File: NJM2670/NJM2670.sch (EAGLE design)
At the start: 10 parts, among them Q1 MOSFET-PCHANNELIRLML2244

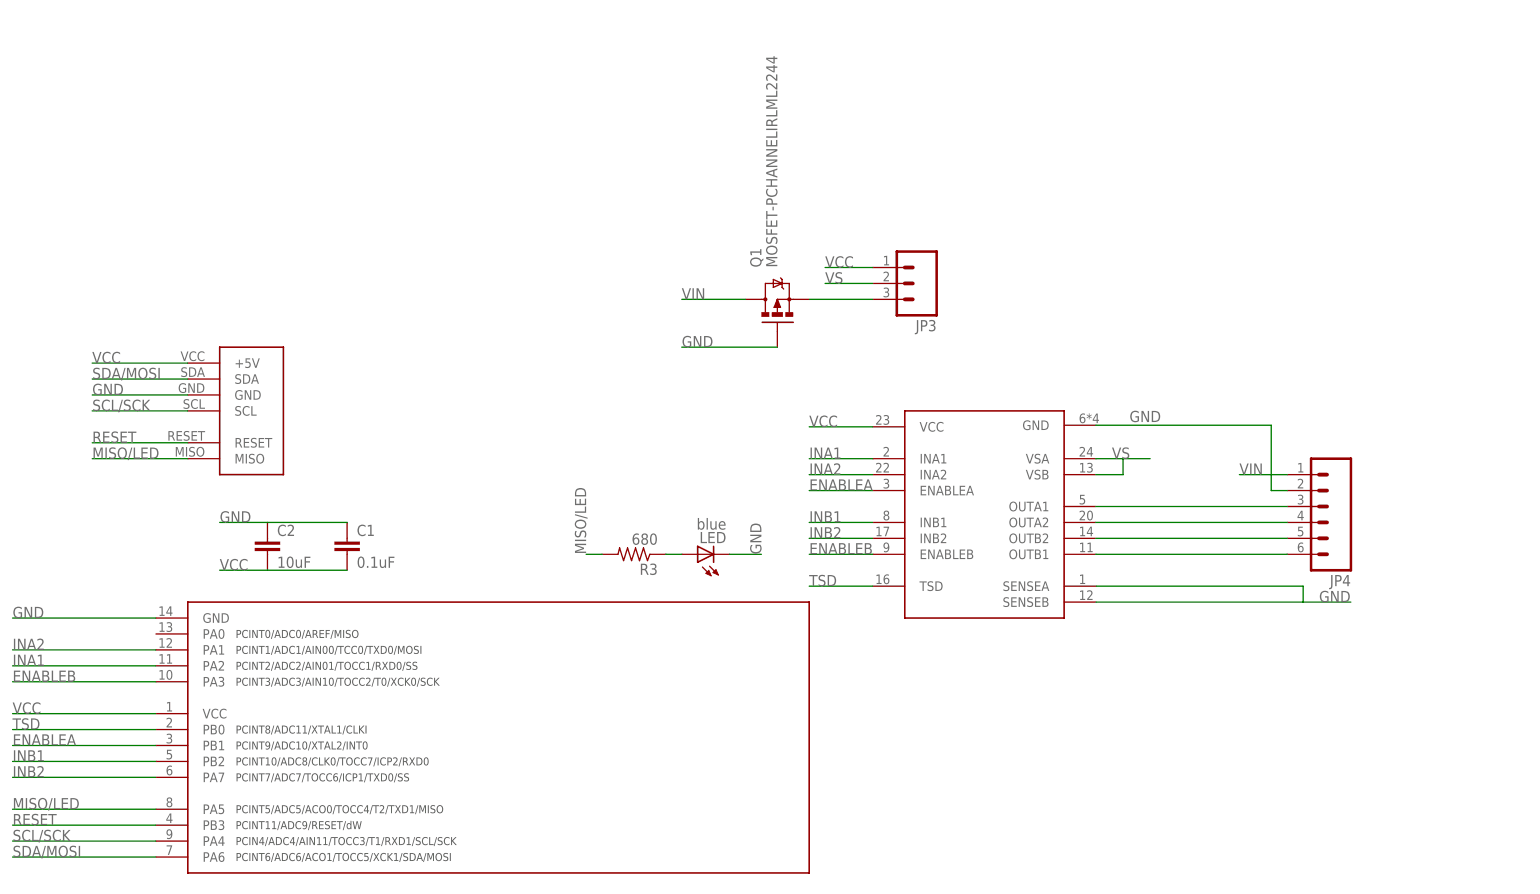
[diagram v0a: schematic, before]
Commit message: New linear/inline layout of motor driver board
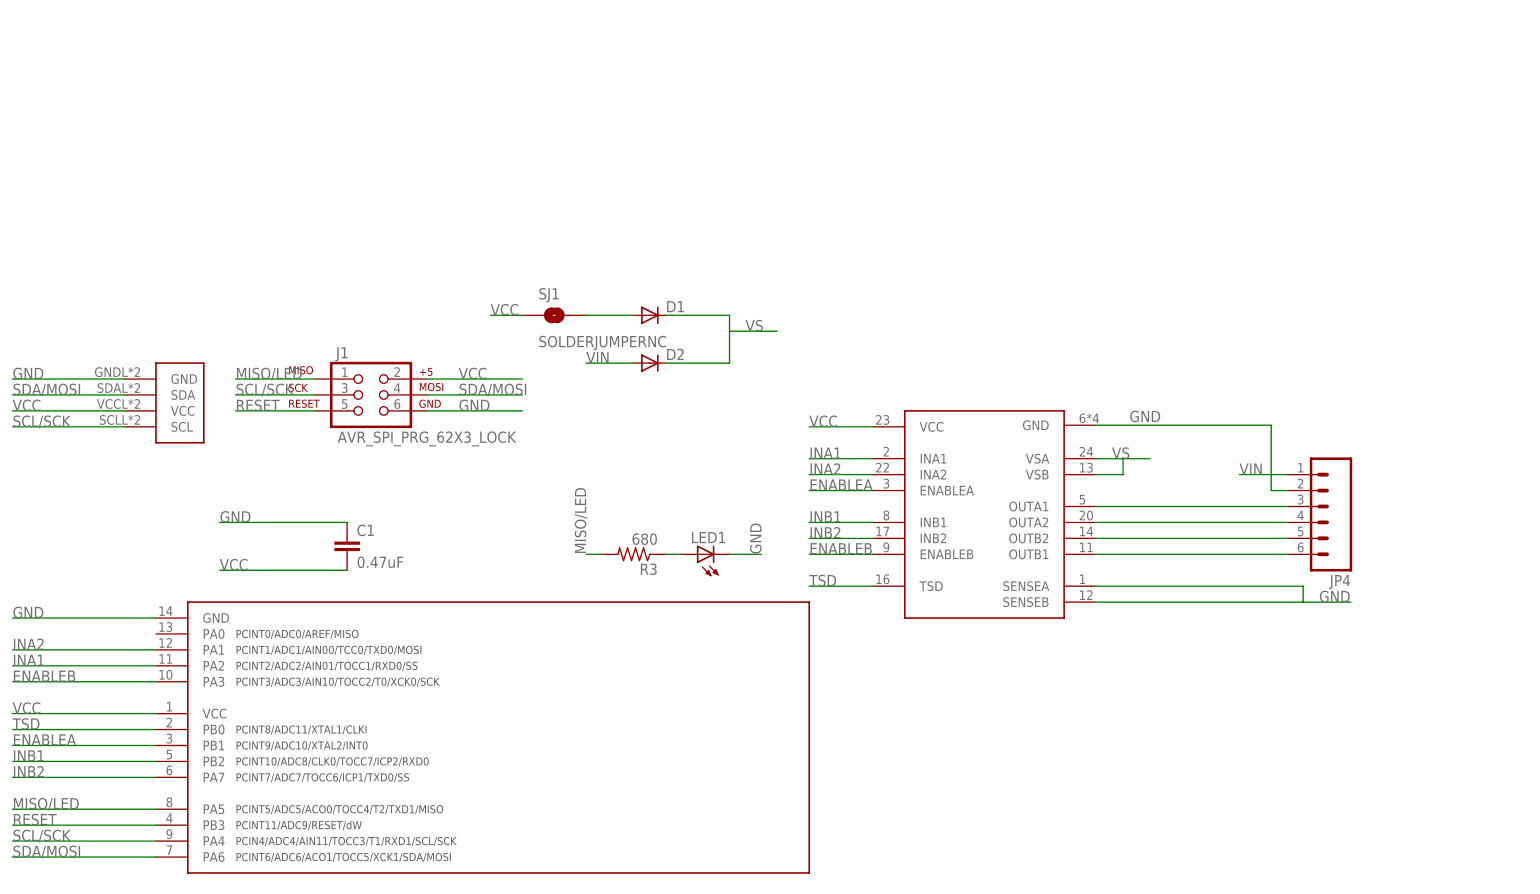
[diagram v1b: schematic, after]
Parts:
- removed C2: 10uF, SparkFun-Capacitors:CAP0805
- removed JP3: (no value), SparkFun-Connectors:M03PTH
- removed LED: blue, led:LEDCHIPLED_1206
- removed Q1: MOSFET-PCHANNELIRLML2244, SparkFun-DiscreteSemi:MOSFET-PCHANNELIRLML2244
- removed U$4: FOOTPRINTFOOTPRINT-2, IntegerLabs:FOOTPRINTFOOTPRINT-2
- added D1, D2: (no value), SparkFun-DiscreteSemi:DIODESMB
- added J1: AVR_SPI_PRG_62X3_LOCK, SparkFun-Connectors:AVR_SPI_PRG_62X3_LOCK
- added LED1: (no value), adafruit:LEDCHIPLED_0805
- added SJ1: SOLDERJUMPERNC, SparkFun-Passives:SOLDERJUMPERNC
- added U$1: FOOTPRINT3-4U, IntegerLabs:FOOTPRINT3-4U
- C1: value 0.1uF -> 0.47uF
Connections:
- net GND: now also J1.6, LED1.C, U$1.GND; no longer C2.1, LED.C, Q1.G, U$4.GND
- net MISO/LED: now also J1.1; no longer U$4.MISO
- net N$1: now also D1.A, SJ1.2; no longer JP3.3, Q1.S
- net N$5: now also LED1.A; no longer LED.A
- net RESET: now also J1.5; no longer U$4.RESET
- net SCL/SCK: now also J1.3, U$1.SCL; no longer U$4.SCL
- net SDA/MOSI: now also J1.4, U$1.SDA; no longer U$4.SDA
- net VCC: now also J1.2, SJ1.1, U$1.VCC; no longer C2.2, JP3.1, U$4.+5V
- net VIN: now also D2.A; no longer Q1.D
- net VS: now also D1.C, D2.C; no longer JP3.2

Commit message: Reverted to old version of motor driver board
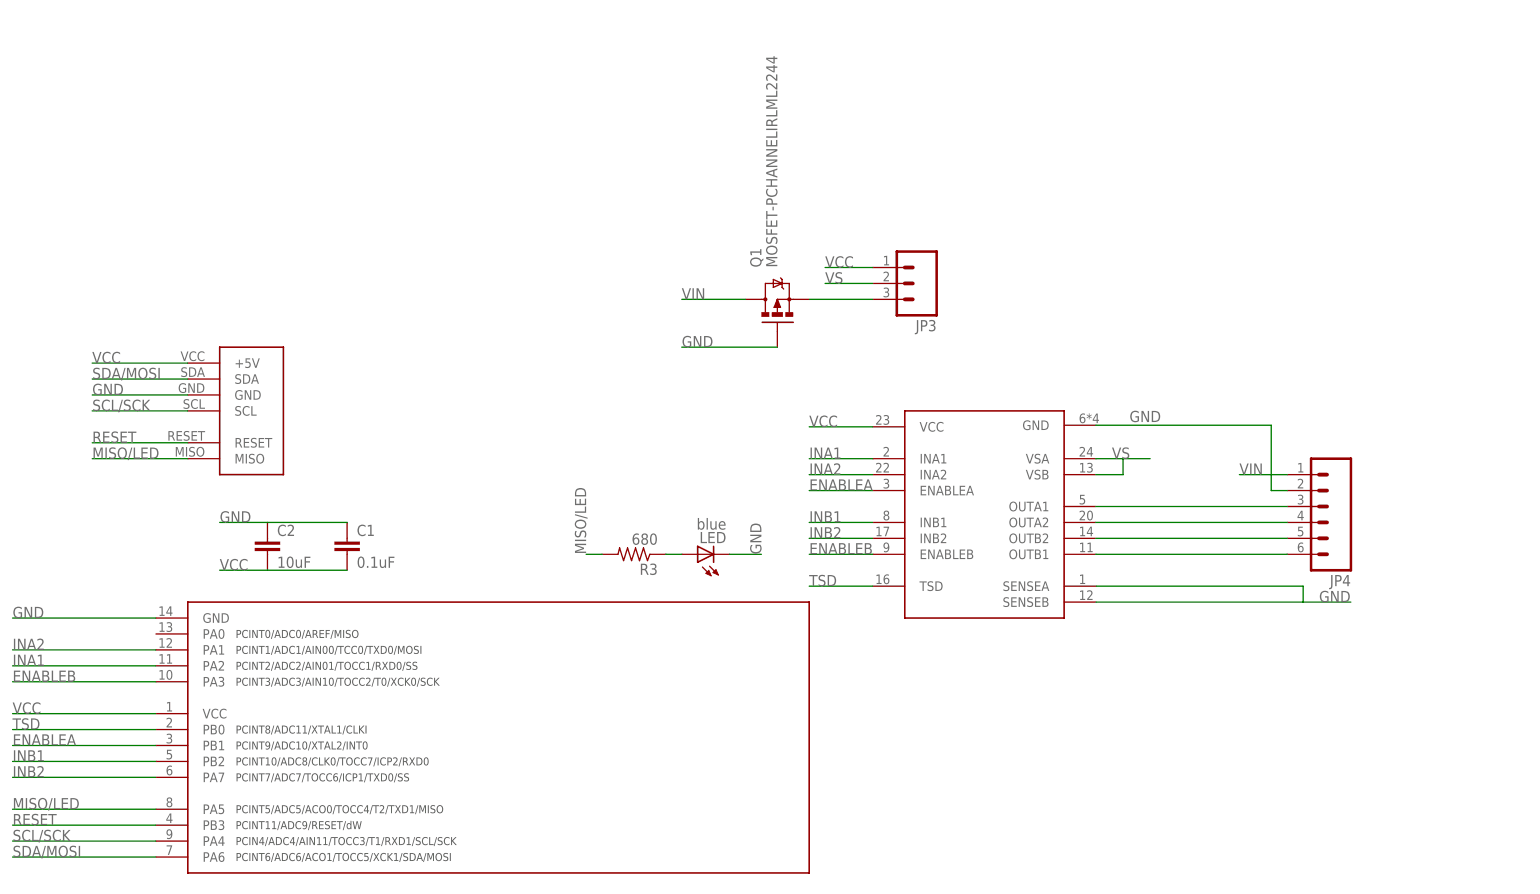
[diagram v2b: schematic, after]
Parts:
- removed D1, D2: (no value), SparkFun-DiscreteSemi:DIODESMB
- removed J1: AVR_SPI_PRG_62X3_LOCK, SparkFun-Connectors:AVR_SPI_PRG_62X3_LOCK
- removed LED1: (no value), adafruit:LEDCHIPLED_0805
- removed SJ1: SOLDERJUMPERNC, SparkFun-Passives:SOLDERJUMPERNC
- removed U$1: FOOTPRINT3-4U, IntegerLabs:FOOTPRINT3-4U
- added C2: 10uF, SparkFun-Capacitors:CAP0805
- added JP3: (no value), SparkFun-Connectors:M03PTH
- added LED: blue, led:LEDCHIPLED_1206
- added Q1: MOSFET-PCHANNELIRLML2244, SparkFun-DiscreteSemi:MOSFET-PCHANNELIRLML2244
- added U$4: FOOTPRINTFOOTPRINT-2, IntegerLabs:FOOTPRINTFOOTPRINT-2
- C1: value 0.47uF -> 0.1uF
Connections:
- net GND: now also C2.1, LED.C, Q1.G, U$4.GND; no longer J1.6, LED1.C, U$1.GND
- net MISO/LED: now also U$4.MISO; no longer J1.1
- net N$1: now also JP3.3, Q1.S; no longer D1.A, SJ1.2
- net N$5: now also LED.A; no longer LED1.A
- net RESET: now also U$4.RESET; no longer J1.5
- net SCL/SCK: now also U$4.SCL; no longer J1.3, U$1.SCL
- net SDA/MOSI: now also U$4.SDA; no longer J1.4, U$1.SDA
- net VCC: now also C2.2, JP3.1, U$4.+5V; no longer J1.2, SJ1.1, U$1.VCC
- net VIN: now also Q1.D; no longer D2.A
- net VS: now also JP3.2; no longer D1.C, D2.C

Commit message: Updated footprint and swich, instead of jumper, for selecting output voltage.
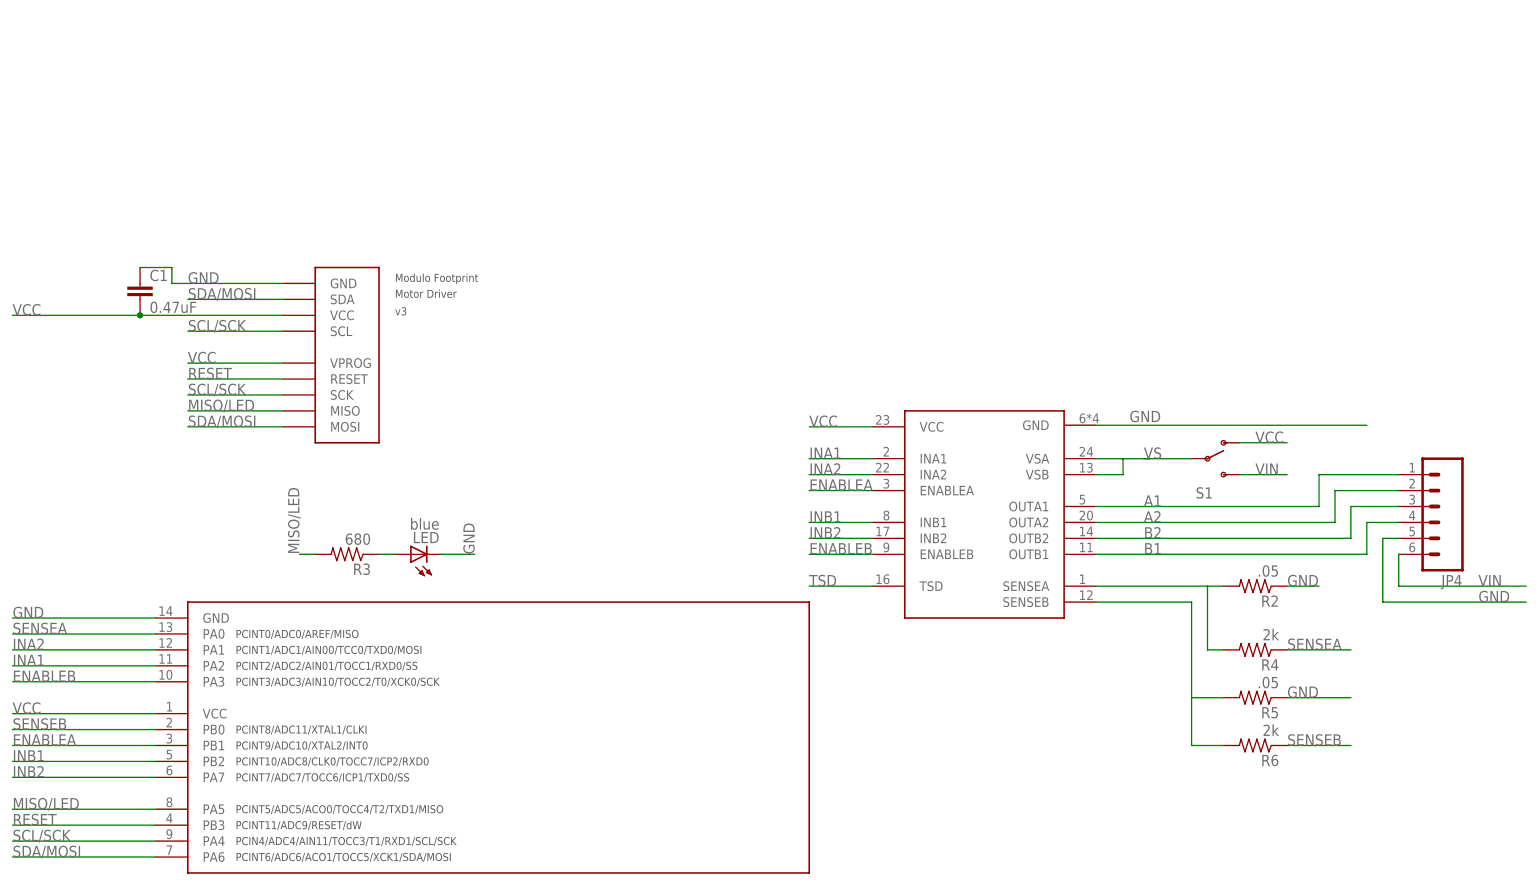
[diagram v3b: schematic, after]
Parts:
- removed C2: 10uF, SparkFun-Capacitors:CAP0805
- removed JP3: (no value), SparkFun-Connectors:M03PTH
- removed Q1: MOSFET-PCHANNELIRLML2244, SparkFun-DiscreteSemi:MOSFET-PCHANNELIRLML2244
- removed U$4: FOOTPRINTFOOTPRINT-2, IntegerLabs:FOOTPRINTFOOTPRINT-2
- added R2, R5: .05, SparkFun-Passives:RESISTOR0805-RES
- added R4, R6: 2k, SparkFun-Passives:RESISTOR0805-RES
- added S1: (no value), SparkFun-Electromechanical:SWITCH-SPDTPTH_LOCK
- added U$1: FOOTPRINTFOOTPRINT-2, IntegerLabs:FOOTPRINTFOOTPRINT-2
- C1: value 0.1uF -> 0.47uF
- LED: device led:LEDCHIPLED_1206 -> adafruit:LEDCHIPLED_0805
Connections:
- removed net N$1: JP3.3, Q1.S
- removed net N$11: JP4.3, U$6.OUTA1
- removed net N$12: JP4.4, U$6.OUTA2
- removed net N$13: JP4.5, U$6.OUTB2
- removed net N$14: JP4.6, U$6.OUTB1
- new net A1: JP4.1, U$6.OUTA1
- new net A2: JP4.2, U$6.OUTA2
- new net B1: JP4.4, U$6.OUTB1
- new net B2: JP4.3, U$6.OUTB2
- new net N$2: R2.2, R4.2, U$6.SENSEA
- new net N$3: R5.2, R6.2, U$6.SENSEB
- new net SENSEA: R4.1, U$3.PA0
- new net SENSEB: R6.1, U$3.PB0
- net GND: now also JP4.5, R2.1, R5.1, U$1.GND; no longer C2.1, JP4.2, Q1.G, U$4.GND, U$6.SENSEA, U$6.SENSEB
- net MISO/LED: now also U$1.MISO; no longer U$4.MISO
- net RESET: now also U$1.RESET; no longer U$4.RESET
- net SCL/SCK: now also U$1.SCK, U$1.SCL; no longer U$4.SCL
- net SDA/MOSI: now also U$1.MOSI, U$1.SDA; no longer U$4.SDA
- net TSD: no longer U$3.PB0
- net VCC: now also S1.O, U$1.VCC, U$1.VPROG; no longer C2.2, JP3.1, U$4.+5V
- net VIN: now also JP4.6, S1.S; no longer JP4.1, Q1.D
- net VS: now also S1.P; no longer JP3.2
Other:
- moved on the sheet: C1, JP4, LED, R3

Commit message: Checkpointing PCB designs
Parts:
- removed S1: (no value), SparkFun-Electromechanical:SWITCH-SPDTPTH_LOCK
- added C2: (no value), SparkFun-Capacitors:CAP_POLC
- added C3, C4, C5: 0.47uF, SparkFun-Capacitors:CAP0805
- added D1, D2: (no value), SparkFun-DiscreteSemi:DIODESMA
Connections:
- net INA1 renamed IN0
- net INA2 renamed IN1
- net INB1 renamed IN2
- net INB2 renamed IN3
- removed net A1: JP4.1, U$6.OUTA1
- removed net A2: JP4.2, U$6.OUTA2
- removed net B1: JP4.4, U$6.OUTB1
- removed net B2: JP4.3, U$6.OUTB2
- new net OUT0: JP4.4, U$6.OUTA1
- new net OUT1: JP4.3, U$6.OUTA2
- new net OUT2: JP4.5, U$6.OUTB2
- new net OUT3: JP4.6, U$6.OUTB1
- net GND: now also C2.-, C3.2, C4.2, C5.2, JP4.1; no longer JP4.5
- net SENSEA: now also C4.1
- net SENSEB: now also C5.1
- net VCC: now also C3.1, D1.A; no longer S1.O
- net VIN: now also D2.A, JP4.2; no longer JP4.6, S1.S
- net VS: now also C2.+, D1.C, D2.C; no longer S1.P
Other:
- moved on the sheet: JP4
